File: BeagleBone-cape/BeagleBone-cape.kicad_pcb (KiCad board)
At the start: 4 copper layers, 86.4 x 54.6 mm, 104 parts, among them IC1 A6983C50QTR, IC2 TCAN3413DDFR, IC3 BMP390, IC4 BMM350, J1 Servo 0, J10 MotorR, J11 CAN, J12 24V, J13 MAVLink, J2 Servo 1, J3 Servo 2, J4 Servo 3, J5 LEDL, J6 LEDR, J7 MAG_I2C_TP, J8 Air Speed Sensor, J9 MotorL, P8 BeagleBone_Black_Header, P9 BeagleBone_Black_Header, Q2 Q_NMOS_GSD, U2 BHI360, U3 DS1307ZN+, Y1 32.768kHz

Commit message: Add i2c logic level translator
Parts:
- removed D3: D_Small, Diode_SMD:D_0603_1608Metric
- added C19: 100n, Capacitor_SMD:C_0603_1608Metric_Pad1.08x0.95mm_HandSolder, F.Cu at (143.2, 73.7)
- added C20: 1u, Capacitor_SMD:C_0603_1608Metric_Pad1.08x0.95mm_HandSolder, F.Cu at (165.9, 73.8)
- added C21: 1u, Capacitor_SMD:C_0603_1608Metric_Pad1.08x0.95mm_HandSolder, F.Cu at (164.7, 68.0)
- added Q1: DMP3013SFV, Package_SON:Diodes_PowerDI3333-8, F.Cu at (127.8, 76.8)
- added R25: 4k7, Resistor_SMD:R_0603_1608Metric_Pad0.98x0.95mm_HandSolder, F.Cu at (144.4, 76.2)
- added R26: 4k7, Resistor_SMD:R_0603_1608Metric_Pad0.98x0.95mm_HandSolder, F.Cu at (145.9, 73.7)
- added R27: 200k, Resistor_SMD:R_0603_1608Metric_Pad0.98x0.95mm_HandSolder, F.Cu at (149.4, 73.7)
- added U4: TLV75518PDBV, Package_TO_SOT_SMD:SOT-23-5, F.Cu at (164.6, 71.0)
- added U5: PCA9306DCUR, Package_SO:VSSOP-8_2.3x2mm_P0.5mm, F.Cu at (148.6, 75.8)
- added U6: LTC4412ES6, Package_TO_SOT_SMD:TSOT-23-6, F.Cu at (123.9, 77.0)
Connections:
- C14 pad 2: Net-(D3-A) -> /Power/BUCK_OUT
- C15 pad 2: Net-(D3-A) -> /Power/BUCK_OUT
- C16 pad 2: Net-(D3-A) -> /Power/BUCK_OUT
- IC1 pad 7: Net-(D3-A) -> +5V
- IC4 pad A2: /I2C_SCL_MAG -> /I2C_SDA_MAG
- IC4 pad A3: /I2C_SDA_MAG -> /I2C_SCL_MAG
- L1 pad 2: Net-(D3-A) -> /Power/BUCK_OUT
- P9 pad 17: /I2C1.SCL -> /I2C1_3V3.SCL
- P9 pad 18: /I2C1.SDA -> /I2C1_3V3.SDA
- P9 pad 32: +1V8 -> unconnected-(P9-Pin_32-Pad32)
- R18 pad 2: Net-(D3-A) -> /Power/BUCK_OUT
- R22 pad 1: +5V -> +3V3
- R23 pad 1: +5V -> +3V3
- TP17 pad 1: /I2C_SCL_MAG -> /I2C_SDA_MAG
- TP18 pad 1: /I2C_SDA_MAG -> /I2C_SCL_MAG
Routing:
- net /I2C1.SCL: track 45.6 -> 12.1 mm, vias 3 -> 2
- net Net-(D3-A): track 26.0 -> 0.00 mm, vias 25 -> 0
- net /Power/BUCK_OUT: track 0.00 -> 23.6 mm, vias 0 -> 25
- net /I2C_SCL_MAG: track 19.8 -> 3.47 mm, vias 2 -> 1
- net /I2C1.SDA: track 36.1 -> 29.5 mm
- net +1V8: track 37.3 -> 32.8 mm
- net /I2C_SDA_MAG: track 15.8 -> 12.5 mm
- net +5V: track 11.5 -> 9.92 mm, vias 16 -> 15
- net GND: vias 425 -> 406
- added copper zone on B.Cu, net /Power/BUCK_OUT
- added copper zone on F.Cu, net /Power/BUCK_OUT
- removed copper zone on B.Cu, net Net-(D3-A)
- removed copper zone on F.Cu, net Net-(D3-A)

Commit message: Update BeagleBone cape schematic/PCB, drop tracked KiCad backups
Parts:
- moved R25 36.6 mm to (149.9, 40.0)
- moved R26 33.7 mm to (145.1, 40.0)
- moved C21 31.9 mm to (133.9, 76.4), turned to 90 degrees
- moved U4 28.4 mm to (136.7, 76.5), turned to 180 degrees
- moved C20 25.5 mm to (140.5, 75.7)
- moved R18 5.84 mm to (116.2, 81.2), turned to 90 degrees
- moved R27 5.80 mm to (143.9, 75.4), turned to -90 degrees
- moved C19 2.75 mm to (145.4, 75.4)
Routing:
- net /Power/BUCK_OUT: track 23.6 -> 33.6 mm, vias 25 -> 26
- net +1V8: track 32.8 -> 37.9 mm, vias 7 -> 8
- net +3V3: track 33.8 -> 38.7 mm
- net Net-(Q1-G): track 0.00 -> 4.59 mm
- net +5V: track 9.92 -> 13.6 mm, vias 15 -> 22
- net /I2C1_EN: track 0.00 -> 3.35 mm
- net /Power/PGOOD: track 4.13 -> 5.22 mm
- net /I2C2.SCL: track 110.2 -> 109.3 mm
- net GND: vias 406 -> 402

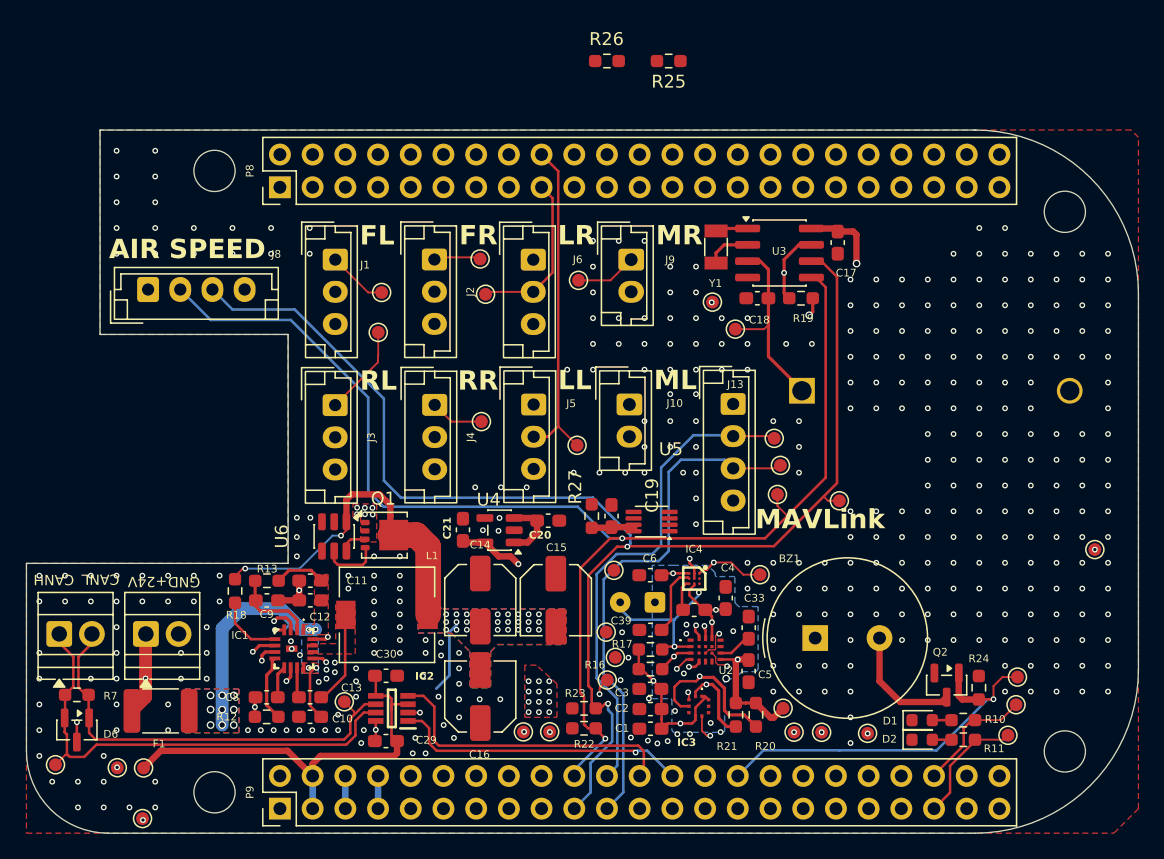
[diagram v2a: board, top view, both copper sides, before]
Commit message: BeagleBone cape: add SN74LVC1T45 level shifters for BHI360 INT/RESET
BHI360 is a 1.8 V device (VDDIO max 1.89 V, abs max VDDIO+0.3 V), while
the AM335x P9 header is 3.3 V LVCMOS. Route INT (U2.4 -> P9.14) through
U7 (A->B, DIR=+1V8) and RESETN (P9.16 -> U2.17) through U8 (B->A,
DIR=GND). R28 10k holds RESET deasserted on the 3.3 V side while the pin
is undriven; C40-C43 decouple both sides.

PCB not yet updated from schematic; new parts still need placement and
routing. Some new parts sit off the 1.27 mm grid.
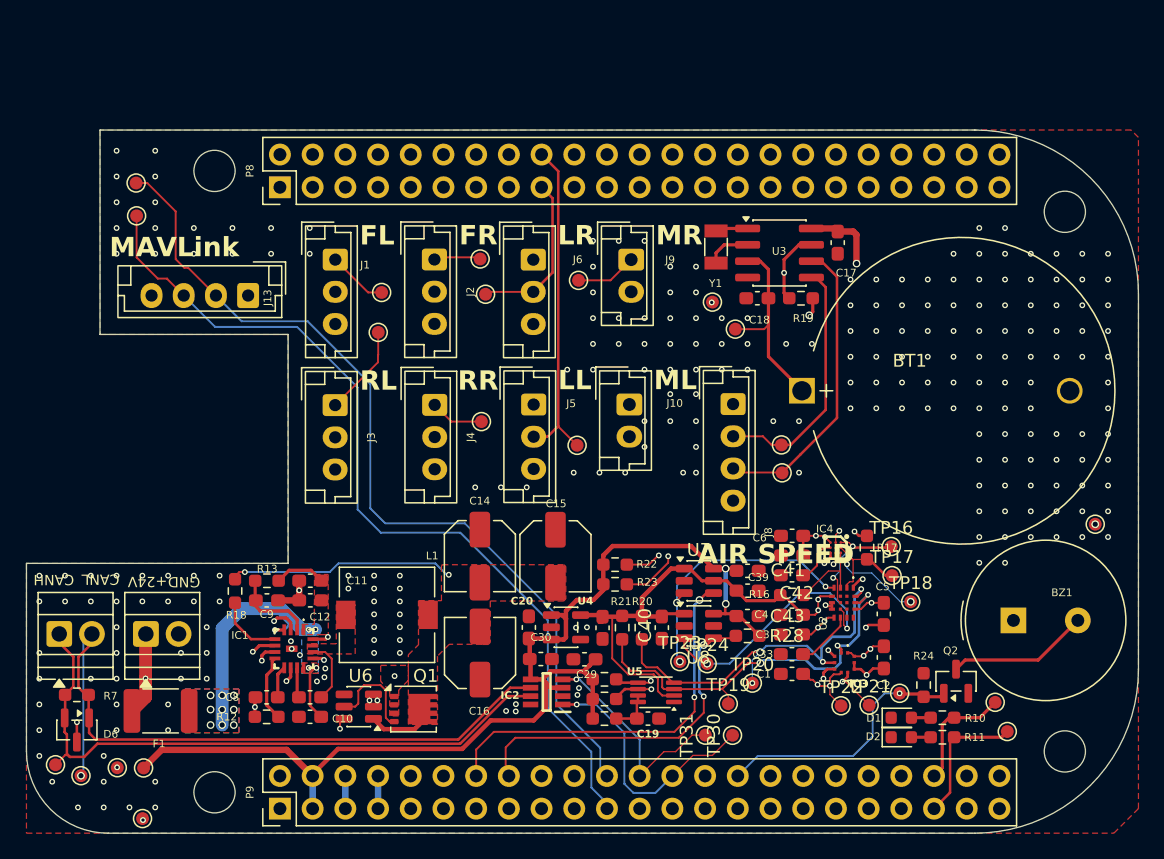
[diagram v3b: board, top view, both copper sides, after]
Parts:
- removed J7: MAG_I2C_TP, Connector_Wire:SolderWire-0.1sqmm_1x02_P3.6mm_D0.4mm_OD1mm
- added C40: 100n, Capacitor_SMD:C_0603_1608Metric_Pad1.08x0.95mm_HandSolder, F.Cu at (149.3, 84.0)
- added C41: 100n, Capacitor_SMD:C_0603_1608Metric_Pad1.08x0.95mm_HandSolder, F.Cu at (156.0, 79.6)
- added C42: 100n, Capacitor_SMD:C_0603_1608Metric_Pad1.08x0.95mm_HandSolder, F.Cu at (156.0, 81.2)
- added C43: 100n, Capacitor_SMD:C_0603_1608Metric_Pad1.08x0.95mm_HandSolder, F.Cu at (156.0, 83.1)
- added R28: 10k, Resistor_SMD:R_0603_1608Metric_Pad0.98x0.95mm_HandSolder, F.Cu at (156.0, 84.7)
- added U7: SN74LVC1T45DBVR, Package_TO_SOT_SMD:SOT-23-6, F.Cu at (152.2, 80.4)
- added U8: SN74LVC1T45DBVR, Package_TO_SOT_SMD:SOT-23-6, F.Cu at (152.2, 83.9)
- BT1: moved to F.Cu
- moved TP15 53.6 mm to (108.6, 52.1)
- moved TP14 53.4 mm to (108.5, 49.5)
- moved R25 49.8 mm to (144.9, 89.6)
- moved R26 48.0 mm to (144.9, 88.0)
- moved J8 46.3 mm to (154.9, 66.7), turned to -90 degrees
- moved J13 38.6 mm to (117.2, 58.2), turned to 180 degrees
- moved TP18 23.8 mm to (168.7, 82.0)
- moved TP17 21.6 mm to (167.2, 80.0)
- moved TP27 21.2 mm to (104.2, 95.5)
- moved R17 18.6 mm to (165.3, 77.8), turned to -90 degrees
- moved C2 18.6 mm to (166.6, 86.3), turned to -90 degrees
- moved C29 16.7 mm to (143.3, 86.5)
- moved C19 16.0 mm to (148.3, 91.1), turned to 0 degrees
- moved R27 15.8 mm to (144.9, 91.1), turned to 0 degrees
- moved BZ1 15.5 mm to (176.7, 83.5)
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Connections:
- P9 pad 14: /BHI360_INT -> /BHI360_INT_3V3
- P9 pad 16: /BHI360_RESET -> /BHI360_RESET_3V3
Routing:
- net /I2C2.SDA: track 105.5 -> 55.8 mm, vias 2 -> 1
- net +3V3: track 38.7 -> 86.5 mm, vias 0 -> 2
- net /I2C2.SCL: track 109.3 -> 61.8 mm, vias 2 -> 1
- net /BHI360_INT_3V3: track 0.00 -> 30.4 mm, vias 0 -> 2
- net /GPIO2: track 38.6 -> 68.5 mm
- net /GPIO3: track 40.5 -> 68.9 mm
- net /BHI360_RESET_3V3: track 0.00 -> 27.1 mm, vias 0 -> 2
- net /CAN-: track 34.4 -> 56.3 mm, vias 0 -> 1
- net +1V8: track 37.9 -> 59.8 mm, vias 8 -> 13
- net /FDCAN_RX: track 37.8 -> 17.1 mm
- net /I2C1.SCL: track 12.1 -> 31.5 mm, vias 2 -> 3
- net /I2C1_3V3.SCL: track 0.00 -> 17.7 mm, vias 0 -> 1
- net /FDCAN_TX: track 37.2 -> 20.2 mm, vias 2 -> 1
- net /I2C1_3V3.SDA: track 0.00 -> 15.5 mm, vias 0 -> 1
- net /INT: track 15.9 -> 3.69 mm, vias 2 -> 1
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- added copper zone on In2.Cu, net +1V8
- removed copper zone on B.Cu, net +1V8
- removed copper zone on B.Cu, net /Power/BUCK_OUT

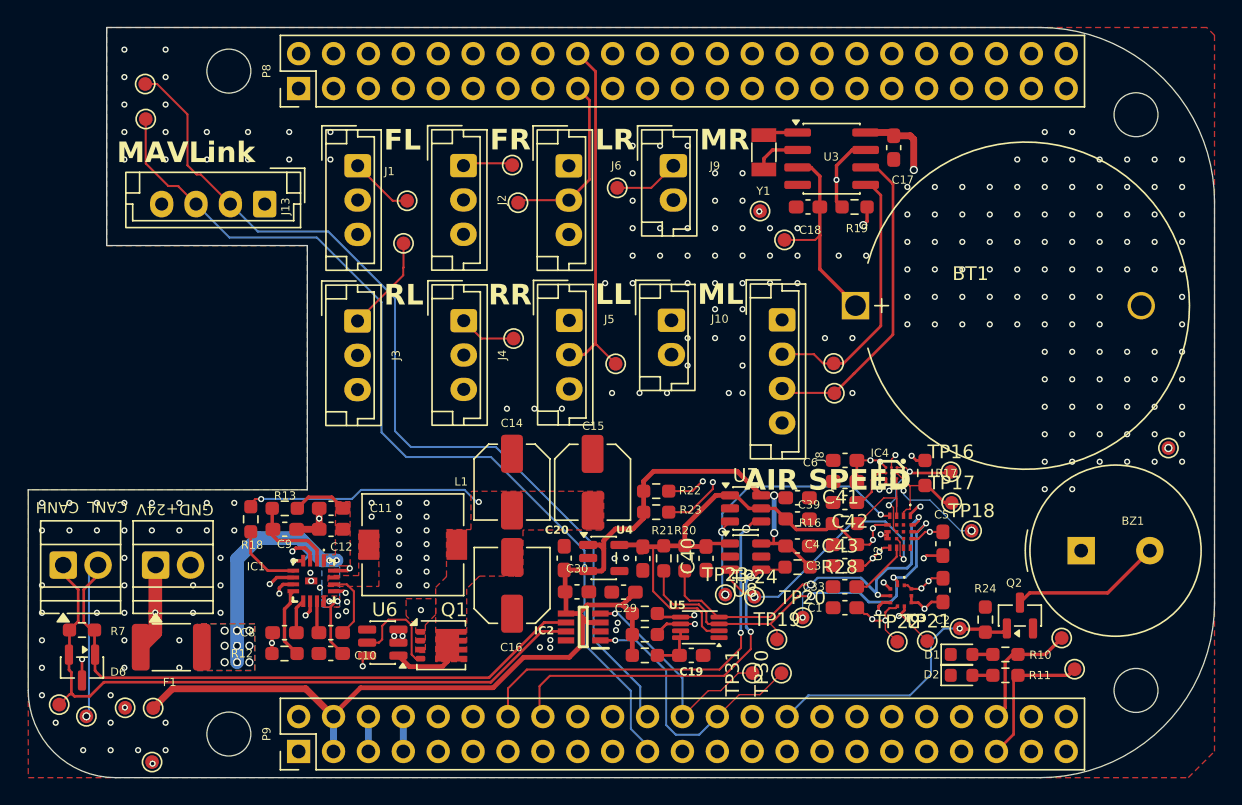
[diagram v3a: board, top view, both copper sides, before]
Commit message: BeagleBone cape: PCB/schematic updates, cape issues list, docs
- Update BeagleBone-cape KiCad schematic and PCB; add BHI360/BMP390 footprint updates
- Add ISSUES.md: cape design review findings (BHI360 1.8V/3.3V level shifting, etc.)
- Ignore .kicad-mcp/ local state
- Update docs/ROADMAP.md and docs/prus.md (PRU1 servo/ESC PWM design); README link
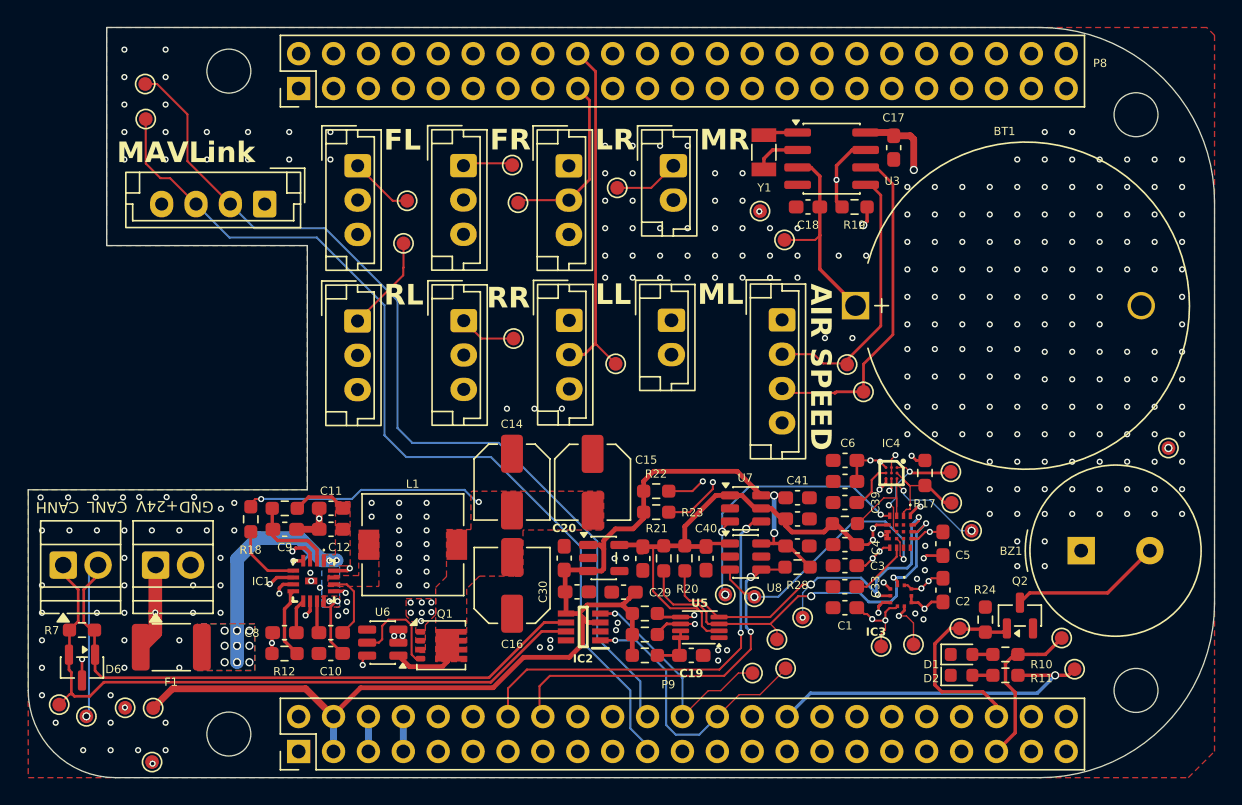
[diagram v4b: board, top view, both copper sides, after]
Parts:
- moved TP13 2.12 mm to (160.8, 71.9)
- moved TP22 1.22 mm to (162.1, 90.4)
- moved TP21 1.03 mm to (164.4, 90.3)
- moved TP12 0.98 mm to (159.6, 69.9)
- moved TP30 0.46 mm to (155.1, 92.0)
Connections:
- P9 pad 30: /BUZZER -> /GPIO20
- P9 pad 41: /GPIO20 -> /GPIO7
- P9 pad 42: /GPIO7 -> /BUZZER
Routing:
- net /GPIO20: track 10.6 -> 25.6 mm, vias 0 -> 1
- net /BUZZER: track 20.3 -> 14.9 mm, vias 1 -> 0
- net /GPIO7: track 8.64 -> 12.8 mm
- net /I2C2.SCL: track 61.8 -> 65.1 mm
- net +1V8: track 59.8 -> 60.8 mm
- net +5V: track 12.4 -> 12.3 mm, vias 6 -> 12
- net GND: vias 260 -> 302

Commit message: Cape: replace BHI360/BMM350 with LSM6DSV16X (SPI1) + IIS2MDC (I2C1)
- Remove BHI360, BMM350 and the 1.8 V domain (TLV75518, PCA9306, SN74LVC1T45 x2)
- Add LSM6DSV16X on SPI1 (P9.28-31), INT1/INT2 on P9.14/P9.16
- Add IIS2MDC on I2C1 (0x1E), DRDY on P9.15; BMP390 moved to 3.3 V on I2C1
- Move LED1 feed from P9.30 to P9.23 (P9.30 is now SPI1 D1)
- PCB: drop removed footprints and orphaned copper; new parts staged, not routed
- ISSUES.md: full cape review (issues 21-38); FUNCTIONS.md hardware mapping
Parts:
- removed C19, C4, C40, C41, C42, C43, C5, C6, C7: 100n, Capacitor_SMD:C_0603_1608Metric_Pad1.08x0.95mm_HandSolder
- removed C20, C21, C3: 1u, Capacitor_SMD:C_0603_1608Metric_Pad1.08x0.95mm_HandSolder
- removed C33: 220n, Capacitor_SMD:C_0603_1608Metric_Pad1.08x0.95mm_HandSolder
- removed C39: 2u2F, Capacitor_SMD:C_0603_1608Metric_Pad1.08x0.95mm_HandSolder
- removed IC4: BMM350, caplib:BGA9C40P3X3_128X128X54
- removed R16, R17, R20, R21: 4k7, Resistor_SMD:R_0603_1608Metric_Pad0.98x0.95mm_HandSolder
- removed R27: 200k, Resistor_SMD:R_0603_1608Metric_Pad0.98x0.95mm_HandSolder
- removed R28: 10k, Resistor_SMD:R_0603_1608Metric_Pad0.98x0.95mm_HandSolder
- removed TP17, TP18, TP22: TestPoint, TestPoint:TestPoint_Pad_D1.0mm
- removed U2: BHI360, caplib:BHI360
- removed U4: TLV75518PDBV, Package_TO_SOT_SMD:SOT-23-5
- removed U5: PCA9306DCUR, Package_SO:VSSOP-8_2.3x2mm_P0.5mm
- removed U7, U8: SN74LVC1T45DBVR, Package_TO_SOT_SMD:SOT-23-6
- added C44: 100n, Capacitor_SMD:C_0603_1608Metric_Pad1.08x0.95mm_HandSolder, F.Cu at (-4.07, 108.0)
- added C45: 100n, Capacitor_SMD:C_0603_1608Metric_Pad1.08x0.95mm_HandSolder, F.Cu at (1.93, 108.0)
- added C46: 100n, Capacitor_SMD:C_0603_1608Metric_Pad1.08x0.95mm_HandSolder, F.Cu at (7.93, 108.0)
- added C47: 100n, Capacitor_SMD:C_0603_1608Metric_Pad1.08x0.95mm_HandSolder, F.Cu at (13.9, 108.0)
- added C48: 220n, Capacitor_SMD:C_0603_1608Metric_Pad1.08x0.95mm_HandSolder, F.Cu at (19.9, 108.0)
- added U10: IIS2MDC, Package_LGA:LGA-12_2x2mm_P0.5mm, F.Cu at (25.9, 108.0)
- added U9: LSM6DSV16X, Package_LGA:LGA-14_3x2.5mm_P0.5mm_LayoutBorder3x4y, F.Cu at (31.9, 108.0)
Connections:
- net /INT renamed /BARO_INT
- C1 pad 1: +1V8 -> +3V3
- C2 pad 1: +1V8 -> +3V3
- IC3 pad 1: +1V8 -> +3V3
- IC3 pad 10: +1V8 -> +3V3
- IC3 pad 6: +1V8 -> +3V3
- P9 pad 14: /BHI360_INT_3V3 -> /IMU_INT1
- P9 pad 15: /GPIO48 -> /MAG_DRDY
- P9 pad 16: /BHI360_RESET_3V3 -> /IMU_INT2
- P9 pad 17: /I2C1_3V3.SCL -> /I2C1.SCL
- P9 pad 18: /I2C1_3V3.SDA -> /I2C1.SDA
- P9 pad 30: /GPIO20 -> /SPI1.D1
- R11 pad 2: /GPIO20 -> /GPIO49
- R25 pad 2: /I2C1_3V3.SCL -> /I2C1.SCL
- R26 pad 2: /I2C1_3V3.SDA -> /I2C1.SDA
- TP16 pad 1: /JTAG_DIO -> /MAG_DRDY
- TP23 pad 1: /BHI360_INT -> /IMU_INT1
- TP24 pad 1: /BHI360_RESET -> /IMU_INT2
- TP33 pad 1: /GPIO20 -> /GPIO49
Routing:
- net +1V8: track 60.8 -> 0.00 mm, vias 13 -> 0
- net /BHI360_INT_3V3: track 30.4 -> 0.00 mm, vias 2 -> 0
- net /BHI360_RESET_3V3: track 27.1 -> 0.00 mm, vias 2 -> 0
- net /GPIO20: track 25.6 -> 0.00 mm, vias 1 -> 0
- net /BHI360_INT: track 21.1 -> 0.00 mm, vias 3 -> 0
- net /BHI360_RESET: track 19.8 -> 0.00 mm, vias 2 -> 0
- net /IMU_INT1: track 0.00 -> 19.3 mm, vias 0 -> 2
- net /I2C1_3V3.SCL: track 17.7 -> 0.00 mm, vias 1 -> 0
- net /I2C1_3V3.SDA: track 15.5 -> 0.00 mm, vias 1 -> 0
- net /I2C1.SDA: track 30.5 -> 15.5 mm, vias 4 -> 1
- net /I2C_SCL_MAG: track 14.4 -> 0.00 mm, vias 2 -> 0
- net /JTAG_DIO: track 9.47 -> 0.00 mm, vias 2 -> 0
- net /I2C_SDA_MAG: track 8.09 -> 0.00 mm
- net +3V3: track 86.5 -> 80.9 mm, vias 2 -> 12
- net /GPIO49: track 0.00 -> 4.86 mm
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- added copper zone on In2.Cu, net +3V3
- removed copper zone on In2.Cu, net +1V8
